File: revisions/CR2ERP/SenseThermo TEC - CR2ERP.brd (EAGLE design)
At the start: 63.5 x 45.7 mm, 61 parts, among them Q1 mmbt2222, Q3 6.5A/30V/38mΩ, U1 MIC5225-3.3, U2 AT21CS01, U3 MAX31865, U4 MAX31865, U5 MAX31865, U6 MAX31865, U8 VNH5019

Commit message: Remove 5v to 3v regulator (will be replaced by 12v to 3v regulator.  Change TEC PWM pin.
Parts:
- removed C1, C2: 10uF, microbuilder:1206
- removed J1: (no value), SparkFun-Connectors:1X12_NO_SILK
- removed J2: (no value), SparkFun-Connectors:1X16_NO_SILK
- removed Q1: mmbt2222, SparkFun-DiscreteSemi:SOT23-3
- removed U1: MIC5225-3.3, microbuilder:SOT23-5
- added J3: FEATHERPTH, CapableRobot:FEATHER-PTH
- R2: value 10k -> 1k
- R3: value 2k -> 1k
- moved R2 14.9 mm to (18.6, 41.0)
- moved R1 13.7 mm to (17.2, 41.0)
- moved R3 2.17 mm to (20.0, 41.0), turned to 90 degrees
- turned R17 to 180 degrees
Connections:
- removed net !EN: J1.4, R1.1
- removed net +5V: C1.1, J1.3, R2.2, U1.1
- removed net N$3: Q1.3, R2.1, U1.3
- new net EN: J3.EN, R1.1
- net +3V3: now also J3.3V3, R2.2; no longer C2.1, R3.2, U1.5
- net CS1: now also J3.4; no longer J1.7
- net CS2: now also J3.3; no longer J1.8
- net CS3: now also J3.2; no longer J1.9
- net CS4: now also J3.1; no longer J1.10
- net ENA: now also J3.11; no longer J2.9
- net ENB: now also J3.12; no longer J2.10
- net FB-RC: now also J3.10; no longer J2.8
- net GND: now also J3.GND, R1.2; no longer C1.2, C2.2, J2.13, Q1.2, U1.2
- net INA: now also J3.14; no longer J2.12
- net INB: now also J3.13; no longer J2.11
- net MISO: now also J3.MISO; no longer J2.4
- net MOSI: now also J3.MOSI; no longer J2.5
- net N$4: now also R2.1, R3.2; no longer Q1.1, R1.2
- net PWM: now also J3.5; no longer J2.7
- net SCLK: now also J3.SCK; no longer J2.6
- net SIO: now also J3.6; no longer J1.5
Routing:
- net !EN: track 23.0 -> 0.00 mm, vias 2 -> 0
- net +5V: track 22.8 -> 0.00 mm
- net PWM: track 32.2 -> 53.1 mm, vias 1 -> 4
- net EN: track 0.00 -> 3.50 mm
- net N$3: track 2.66 -> 0.00 mm
- net GND: track 24.3 -> 21.7 mm, vias 94 -> 91
- net +3V3: track 126.3 -> 124.8 mm
- net SIO: track 10.1 -> 9.25 mm
- net ENB: track 33.7 -> 34.4 mm
- net N$4: track 2.12 -> 1.40 mm
- net VCC: vias 32 -> 33

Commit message: Added 12v to 5v regulator and 5v to 3v regulators.  Changed RTD passives to 0603
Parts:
- removed C24: (no value), CapableRobot:1206
- added C1: 10u 16v, CapableRobot:1206
- added C15, C16, C17, C18: 10u, CapableRobot:0805
- added C19: 22u, CapableRobot:0805
- added C2: 330p, CapableRobot:0603
- added R12, R13: 100k, CapableRobot:0603
- added R14: 19.1k, CapableRobot:0603
- added R15: 5.6, CapableRobot:0603
- added R16, R22: 10k, CapableRobot:0603
- added U1: (no value), CapableRobot:QFN50P300X500X165-20
- added U7, U9: 3v3, CapableRobot:SOT25
- C10, C12, C13, C3, C4, C6, C7, C9: value 0.1uF -> 100n; device microbuilder:_0805MP -> CapableRobot:0603
- C11, C14, C5, C8: value 10nF -> 10n; device microbuilder:_0805MP -> CapableRobot:0603
- FB1, FB2, FB3, FB4: device microbuilder:_0805MP -> CapableRobot:0603
- LOGO1: value CRC-LOGO10 -> CRC-LOGO7; device CapableRobot:CRC-LOGO-10 -> CapableRobot:CRC-LOGO-7
- R11, R5, R7, R9: value 4300Ω 0.1% -> 4k3 0.1%; device microbuilder:_0805MP -> CapableRobot:0603
- moved FB2 3.40 mm to (28.4, 27.4), flipped to the top
- moved FB1 3.23 mm to (19.0, 27.4), flipped to the top, turned to 0 degrees
- moved FB3 3.03 mm to (38.5, 27.4), flipped to the top, turned to 0 degrees
- moved FB4 2.97 mm to (45.2, 26.9), flipped to the top, turned to 180 degrees
- moved C7 2.40 mm to (28.4, 28.5), flipped to the top
- moved C13 2.37 mm to (47.2, 28.2), flipped to the top
- moved C4 2.10 mm to (19.0, 28.4), flipped to the top, turned to 0 degrees
- moved R7 1.91 mm to (29.9, 31.6)
- moved LOGO1 1.80 mm to (9.52, 36.8)
- moved C10 1.76 mm to (38.5, 28.4), flipped to the top, turned to 0 degrees
- moved R9 1.12 mm to (39.7, 30.8)
- moved R11 0.58 mm to (49.3, 31.0)
- moved C12 0.53 mm to (44.5, 28.2)
- moved C5 0.50 mm to (17.4, 36.5)
- moved C11 0.40 mm to (36.4, 36.7)
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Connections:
- new net +5V: C15.P$2, C17.P$2, C19.P$2, R13.2, R16.1, R22.1, U1.8, U7.1, U9.1
- new net FBMPM: R13.1, R14.2, U1.1
- new net N$18: C2.2, R15.2
- new net N$20: R16.2, U9.3
- new net N$23: R22.2, U7.3
- new net N$3: R12.1, U1.17
- new net SNUB: R15.1, U1.5
- new net VREGHOST: C18.P$2, J3.3V3, R20.2, R21.2, U7.5
- net +3V3: now also C16.P$2, U9.5; no longer J3.3V3, R20.2, R21.2
- net GND: now also C1.P$1, C15.P$1, C16.P$1, C17.P$1, C18.P$1, C19.P$1, C2.1, R14.1, U1.12, U1.13, U1.14, U1.3, U7.2, U9.2; no longer C24.P$1
- net VIN: now also C1.P$2, R12.2, U1.16; no longer C24.P$2
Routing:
- net +5V: track 0.00 -> 60.2 mm, vias 0 -> 1
- net +3V3: track 124.8 -> 95.6 mm, vias 6 -> 2
- net VREGHOST: track 0.00 -> 24.9 mm, vias 0 -> 2
- net PWM: track 53.1 -> 36.4 mm
- net CS2: track 22.6 -> 24.9 mm, vias 2 -> 0
- net N$7: track 4.08 -> 2.29 mm, vias 1 -> 0
- net N$23: track 0.00 -> 1.46 mm
- net N$20: track 0.00 -> 1.40 mm
- net N$13: track 3.61 -> 2.36 mm, vias 1 -> 0
- net N$10: track 3.43 -> 2.19 mm, vias 1 -> 0
- net N$18: track 0.00 -> 1.20 mm
- net N$8: track 3.25 -> 2.08 mm
- net N$11: track 3.22 -> 2.07 mm
- net N$16: track 4.13 -> 2.99 mm, vias 1 -> 0
- net N$12: track 2.89 -> 1.99 mm
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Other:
- board text added: "3V"
- board text removed: "!EN"
- board text removed: "Capable Robot Components SenseTemp TEC [CRHVEF]"
- board text removed: "VIN"

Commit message: Added high side switch for fan.  Silkscreen changes.
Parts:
- removed TEC: CONN-2-MFJR-RA, CapableRobot:CONN-MFJR-RA-2X1
- added C24, C25: 22u 16v, CapableRobot:1206
- added R23: 10k, CapableRobot:0603
- added TEC/FAN: CONN-4-MFJR-RA, CapableRobot:CONN-MFJR-RA-2X2
- added U10: NCV8461, CapableRobot:SOIC127P600X175-8
- Q3: device SparkFun-DiscreteSemi:SO08 -> CapableRobot:SOIC127P600X175-8
- moved C23 9.18 mm to (35.7, 16.4), turned to 270 degrees
- moved C22 8.91 mm to (38.4, 16.4), turned to 270 degrees
- moved R14 2.93 mm to (52.5, 25.0)
- moved R13 0.76 mm to (51.4, 25.0)
- moved PWR 0.58 mm to (59.0, 16.5)
- moved Q3 0.50 mm to (16.0, 13.9), turned to 0 degrees
- moved R15 0.42 mm to (53.7, 25.0)
- moved C21 0.40 mm to (49.0, 11.8)
- moved C2 0.36 mm to (54.8, 25.0)
- moved C19 0.20 mm to (57.6, 24.7)
- moved C1 0.10 mm to (56.4, 20.2)
- moved R12 0.10 mm to (53.6, 20.2)
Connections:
- new net AGND: R14.1, U1.3
- new net FANCTRL: J3.TX, R23.2, U10.2
- new net FANPWR: C24.P$2, C25.P$2, TEC/FAN.2, U10.3
- new net FANSTAT: J3.RX, U10.4
- net GND: now also C24.P$1, C25.P$1, R23.1, TEC/FAN.4, U10.1; no longer R14.1, U1.3
- net TECM: now also TEC/FAN.3; no longer TEC.2
- net TECP: now also TEC/FAN.1; no longer TEC.1
- net VIN: now also U10.5, U10.6, U10.7, U10.8
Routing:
- net FANCTRL: track 0.00 -> 30.8 mm, vias 0 -> 1
- net FANSTAT: track 0.00 -> 22.9 mm, vias 0 -> 1
- net FANPWR: track 0.00 -> 22.9 mm
- net VIN: track 27.7 -> 47.4 mm
- net PWM: track 36.4 -> 56.0 mm
- net TECP: track 34.6 -> 42.4 mm
- net GND: track 22.0 -> 29.2 mm, vias 100 -> 121
- net FBMPM: track 0.00 -> 5.64 mm, vias 0 -> 1
- net TECM: track 16.1 -> 21.0 mm
- net +5V: track 60.2 -> 63.4 mm, vias 1 -> 2
- net AGND: track 0.00 -> 2.79 mm, vias 0 -> 1
- net SNUB: track 0.00 -> 1.63 mm, vias 0 -> 1
- net N$3: track 0.00 -> 1.20 mm
- added copper zone on layer 16, net +5V
- added copper zone on layer 16, net SNUB
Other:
- board text added: "CTRL"
- board text added: "FAN"
- board text added: "STAT"
- board text added: "SUPPLY"
- board text added: "TEC"

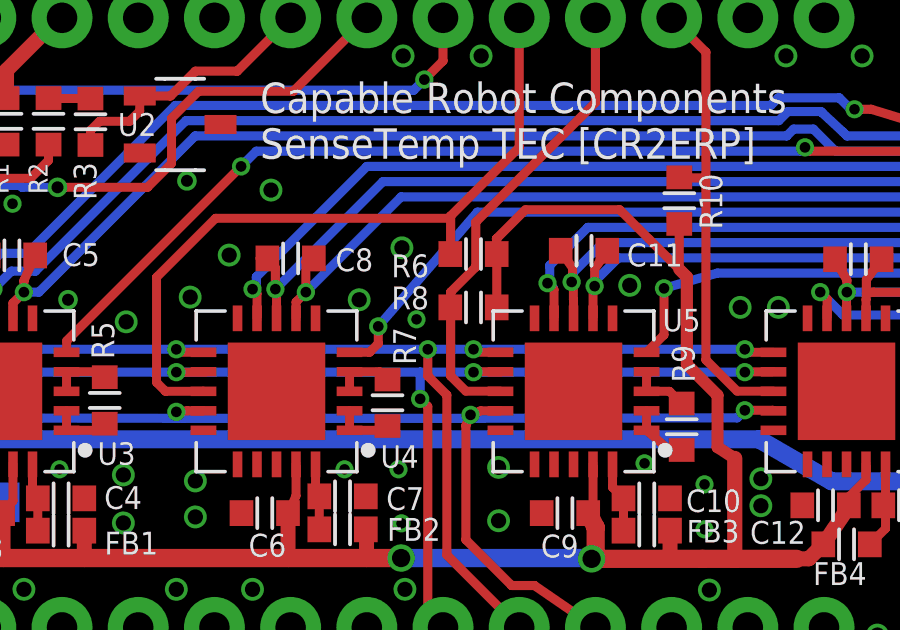
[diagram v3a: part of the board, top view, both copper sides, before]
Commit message: Move R8 away from U5
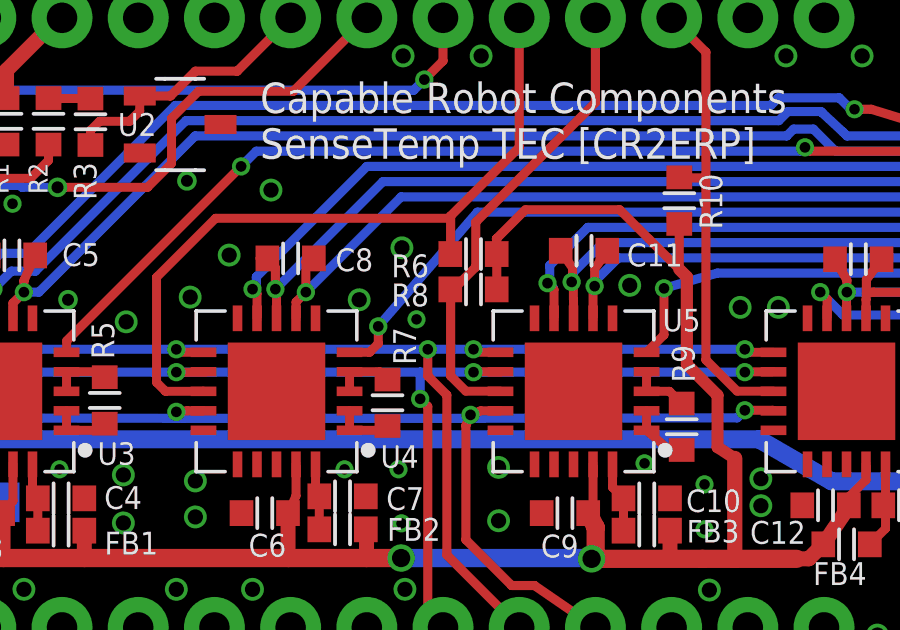
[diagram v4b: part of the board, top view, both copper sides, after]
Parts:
- moved R8 0.60 mm to (32.8, 35.4)
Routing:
- net +3V3: track 95.7 -> 95.1 mm
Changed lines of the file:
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@@
 <layer number="19" name="Unrouted" color="6" fill="1" visible="yes" active="yes"/>
 <layer number="20" name="Dimension" color="15" fill="1" visible="yes" active="yes"/>
-<layer number="21" name="tPlace" color="14" fill="1" visible="no" active="yes"/>
+<layer number="21" name="tPlace" color="14" fill="1" visible="yes" active="yes"/>
 <layer number="22" name="bPlace" color="13" fill="1" visible="yes" active="yes"/>
-<layer number="23" name="tOrigins" color="14" fill="1" visible="no" active="yes"/>
+<layer number="23" name="tOrigins" color="14" fill="1" visible="yes" active="yes"/>
 <layer number="24" name="bOrigins" color="13" fill="1" visible="yes" active="yes"/>
 <layer number="25" name="tNames" color="7" fill="1" visible="yes" active="yes"/>
@@
 <attribute name="NAME" x="30.029" y="35.802" size="0.762" layer="25" font="vector" ratio="15"/>
 </element>
-<element name="R8" library="CapableRobot" package="0603" value="10k" x="32.766" y="34.798" smashed="yes">
-<attribute name="NAME" x="30.029" y="34.732" size="0.762" layer="25" font="vector" ratio="15"/>
+<element name="R8" library="CapableRobot" package="0603" value="10k" x="32.766" y="35.398" smashed="yes">
+<attribute name="NAME" x="30.029" y="34.832" size="0.762" layer="25" font="vector" ratio="15"/>
 </element>
 <element name="R10" library="CapableRobot" package="0603" value="10k" x="39.624" y="38.354" smashed="yes" rot="R270">
@@
 <signal name="CS3">
 <wire x1="32.004" y1="32.512" x2="32.512" y2="32.004" width="0.3048" layer="1"/>
-<wire x1="32.004" y1="34.811" x2="32.004" y2="32.512" width="0.3048" layer="1"/>
+<wire x1="32.004" y1="35.411" x2="32.004" y2="35.306" width="0.3048" layer="1"/>
+<wire x1="32.004" y1="35.306" x2="32.004" y2="32.512" width="0.3048" layer="1"/>
 <contactref element="R8" pad="1"/>
-<wire x1="32.004" y1="34.811" x2="31.991" y2="34.798" width="0.3048" layer="1"/>
-<wire x1="32.004" y1="35.306" x2="32.004" y2="34.811" width="0.3048" layer="1"/>
+<wire x1="32.004" y1="35.411" x2="31.991" y2="35.398" width="0.3048" layer="1"/>
 <wire x1="32.8412" y1="37.64025" x2="32.8412" y2="36.1432" width="0.3048" layer="1"/>
 <wire x1="36.83" y1="44.45" x2="36.83" y2="41.62905" width="0.3048" layer="1"/>
@@
 <wire x1="36.838" y1="27.466" x2="36.589" y2="27.94" width="0.6096" layer="1"/>
 <wire x1="36.838" y1="27.466" x2="36.838" y2="26.416" width="0.6096" layer="1"/>
-<wire x1="33.541" y1="36.576" x2="33.541" y2="34.798" width="0.3048" layer="1"/>
+<wire x1="33.541" y1="36.576" x2="33.541" y2="35.398" width="0.3048" layer="1"/>
 <wire x1="39.624" y1="37.579" x2="39.624" y2="36.068" width="0.3048" layer="1"/>
 <wire x1="33.541" y1="37.071" x2="33.541" y2="36.576" width="0.3048" layer="1"/>

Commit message: Update to released version of CR2ERP
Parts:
- removed C17, C18: 10u, CapableRobot:0805
- removed C2: 330p, CapableRobot:0603
- removed R1: 1k, CapableRobot:0603
- removed R12, R13: 100k, CapableRobot:0603
- removed R14: 19.1k, CapableRobot:0603
- removed R15: 5.6, CapableRobot:0603
- removed R22: 10k, CapableRobot:0603
- removed U9: 3v3, CapableRobot:SOT25
- added C26: 10u, CapableRobot:0805
- added D1: MBR120, Adafruit Feather M0 Express:SOD-123
- C1: value 10u 16v -> 22u 16v
- C19: value 22u -> 10u
- C20: value (none) -> 100n
- C22, C23: value (none) -> 22u 16v
- D3: value SM6J12A -> SMAJ12A
- FB1, FB2, FB3, FB4: value (none) -> 600R
- LOGO1: value CRC-LOGO7 -> CRC-LOGO7SILK; device CapableRobot:CRC-LOGO-7 -> CapableRobot:CRC-LOGO-7-SILK
- R11, R5, R7, R9: value 4k3 0.1% -> 4k3 0.05%
- R17, R19: value 10K -> 10k
- R18: value 1K -> 1k
- U1: value (none) -> NCP1117 3v3; device CapableRobot:QFN50P300X500X165-20 -> CapableRobot:SOT230P700X180-4
- moved C19 5.94 mm to (54.4, 29.7), turned to 0 degrees
- moved U7 4.05 mm to (8.40, 29.8), flipped to the top, turned to 180 degrees
- moved U1 2.75 mm to (57.3, 25.4)
- moved FB4 0.71 mm to (44.5, 26.8)
- moved C1 0.40 mm to (56.8, 20.2)
- moved C13 0.28 mm to (47.4, 28.4)
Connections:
- removed net AGND: R14.1, U1.3
- removed net EN: J3.EN, R1.1
- removed net FBMPM: R13.1, R14.2, U1.1
- removed net N$18: C2.2, R15.2
- removed net N$23: R22.2, U7.3
- removed net N$3: R12.1, U1.17
- removed net SNUB: R15.1, U1.5
- new net VHOST: D1.C, J3.USB
- net +3V3: now also U7.5; no longer U9.5
- net +5V: now also C26.P$2, D1.A, U1.3; no longer C17.P$2, R13.2, R22.1, U1.8, U9.1
- net GND: now also C26.P$1, U1.2, U1.4; no longer C17.P$1, C18.P$1, C2.1, R1.2, U1.12, U1.13, U1.14, U9.2
- net N$20: now also U7.3; no longer U9.3
- net VIN: now also U1.1; no longer R12.2, U1.16
- net VREGHOST: no longer C18.P$2, U7.5
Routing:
- net VHOST: track 0.00 -> 27.1 mm
- net GND: track 29.2 -> 39.8 mm, vias 121 -> 132
- net VIN: track 47.4 -> 55.2 mm
- net +5V: track 63.4 -> 56.3 mm, vias 2 -> 1
- net VREGHOST: track 24.9 -> 18.7 mm
- net FBMPM: track 5.64 -> 0.00 mm, vias 1 -> 0
- net EN: track 3.50 -> 0.00 mm
- net AGND: track 2.79 -> 0.00 mm, vias 1 -> 0
- net SNUB: track 1.63 -> 0.00 mm, vias 1 -> 0
- net N$23: track 1.46 -> 0.00 mm
- net N$3: track 1.20 -> 0.00 mm
- net N$18: track 1.10 -> 0.00 mm
- net FORCE4-: track 15.4 -> 14.8 mm
- removed copper zone on layer 16, net +5V
- removed copper zone on layer 16, net SNUB
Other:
- board text added: "3v3"
- board text added: "5V"
- board text removed: "3V"
